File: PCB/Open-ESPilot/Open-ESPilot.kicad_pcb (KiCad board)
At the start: 2 copper layers, 50.6 x 71.1 mm, 108 parts, among them J1 USB_C_Receptacle_USB2.0_16P, J10 UART1, J11 UART2, J12 I2C, J14 LED out, J2 VOUT, J3 VIN, J4 GND, J5 PWM output, J6 RC in, J7 Vx, J8 GND, J9 UART0, M1 Clone "MP1584" module, M2 GY91, Q1 AO3401A, Q2 BC847, Q3 BC847, SW1 SW_Push, SW2 SW_Push, U1 ESP32-S3-WROOM-1-N8, U2 AMS1117-3.3, U3 AMS1117-3.3, U4 INA219AxD, U5 Micro_SD_Card

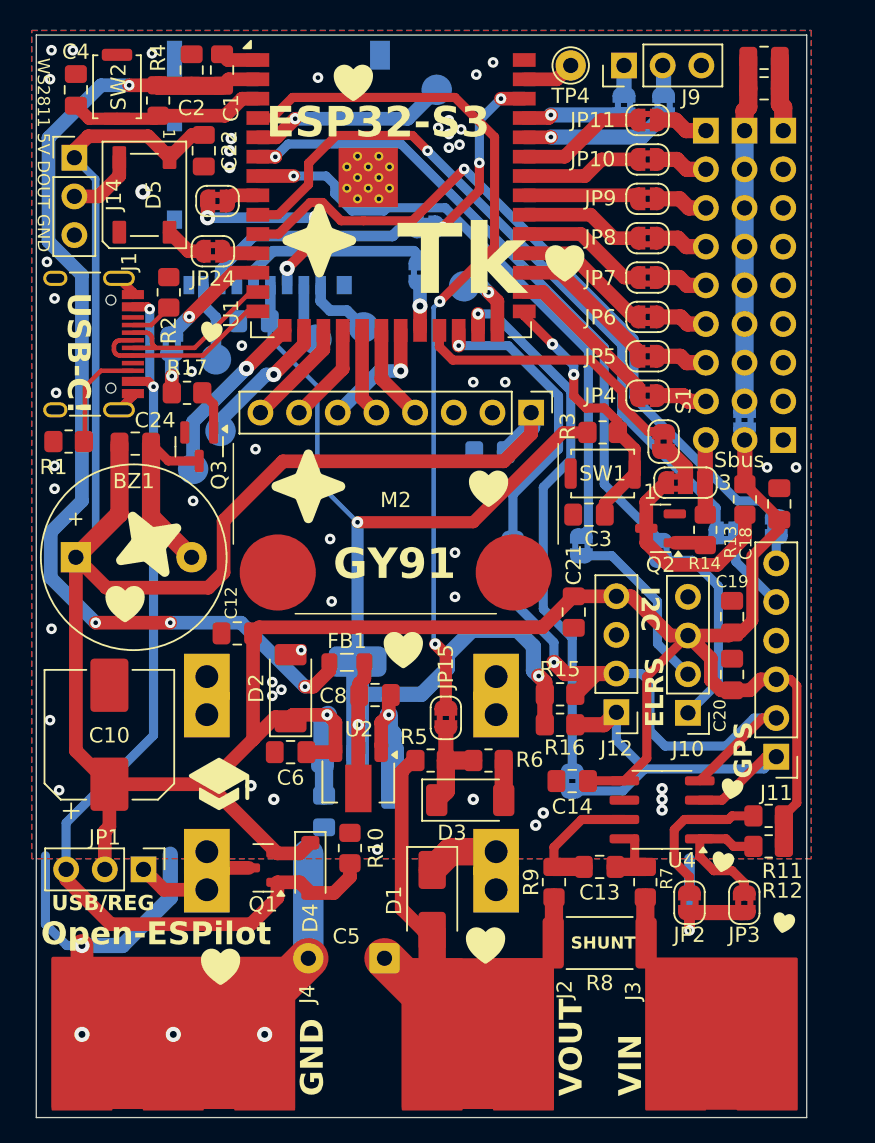
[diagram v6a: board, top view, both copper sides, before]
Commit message: Removed paste layer for PPs and GY-91
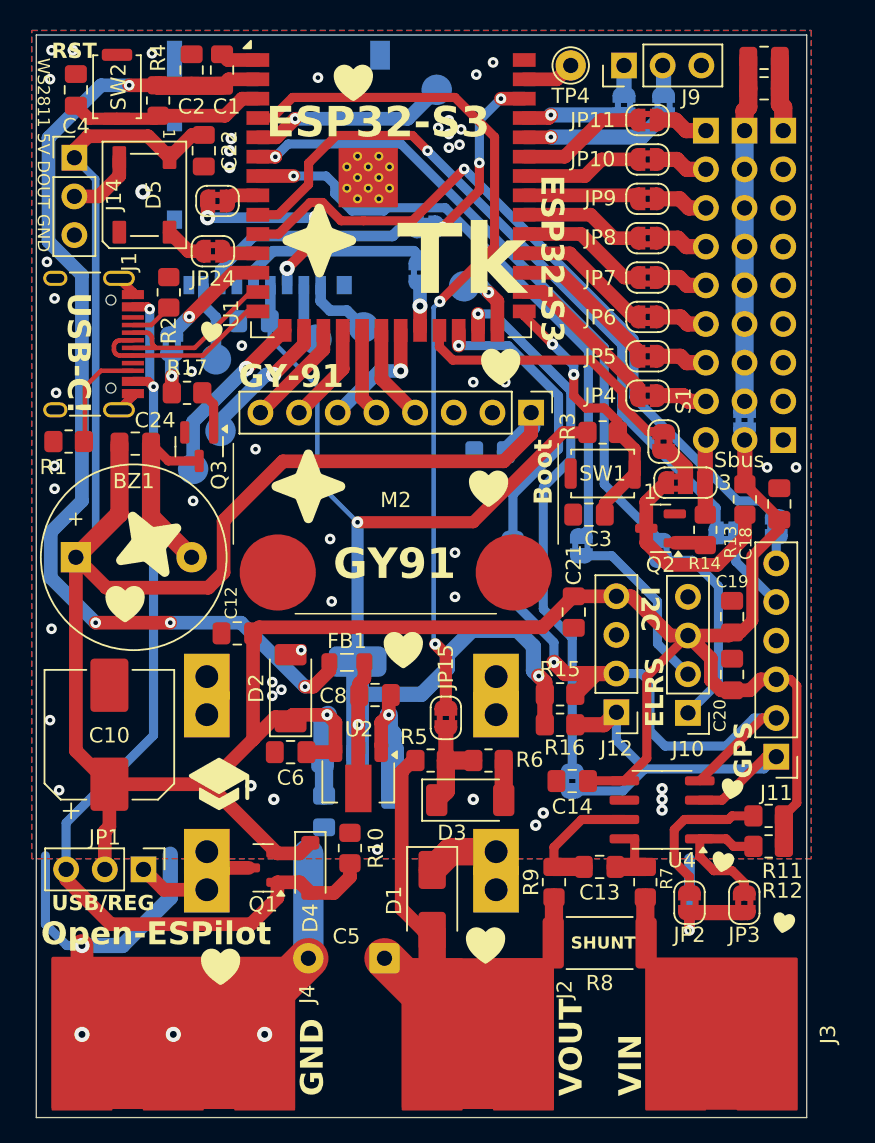
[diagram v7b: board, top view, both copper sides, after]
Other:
- board text added: "Boot"
- board text added: "GY-91"
- board text added: "RST"

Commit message: in dabenginging of V1.1
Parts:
- removed the JP1 at (123.1, 115.1)
- removed JP14: 5V/Vx, Jumper:SolderJumper-2_P1.3mm_Bridged2Bar_RoundedPad1.0x1.5mm
- added D6: 3V3 IG, Diode_SMD:D_SOD-128, F.Cu at (186.9, 79.2)
- added JP4: 5V/Vx, Jumper:SolderJumper-2_P1.3mm_Bridged2Bar_RoundedPad1.0x1.5mm, F.Cu at (185.3, 88.5)
- added JP6: REG/USB, Jumper:SolderJumper-3_P1.3mm_Open_RoundedPad1.0x1.5mm, F.Cu at (122.2, 116.0)
- renumbered JP27 to GJ14, JP26 to GJ15, JP20 to GJ16, JP21 to GJ17, JP24 to GJ18, JP28 to GJ2, JP12 to GJ21, JP4 to GJ35, JP5 to GJ36, JP6 to GJ37, JP7 to GJ38, JP8 to GJ39, JP15 to GJ4, JP9 to GJ40, JP10 to GJ41, JP11 to GJ42, JP16 to GJ43, JP17 to GJ44, JP23 to GJ47, JP22 to GJ48, JP18 to GJ6, JP19 to GJ7, JP25 to GJ8, JP2 to JP1, JP3 to JP2, JP13 to JP5
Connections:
- C10 pad 1: +5V -> +5Vreg
- M1 pad 3: /Power/+5Vreg -> +5Vreg
- Q1 pad 3: /Power/+5Vreg -> +5Vreg
- R13 pad 1: +5V -> +3V3
- U5 pad 10: (no net) -> unconnected-(U5-DET_A-Pad10)
- U5 pad 11: (no net) -> GND
- U5 pad 9: GND -> unconnected-(U5-DET_B-Pad9)
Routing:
- net /Power/+5Vusb: track 65.8 -> 51.8 mm
- net /Power/+5Vreg: track 7.92 -> 0.00 mm
- net +5V: track 235.2 -> 229.4 mm
- net +5Vreg: track 0.00 -> 3.20 mm
